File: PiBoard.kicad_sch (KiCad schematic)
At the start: 0 parts

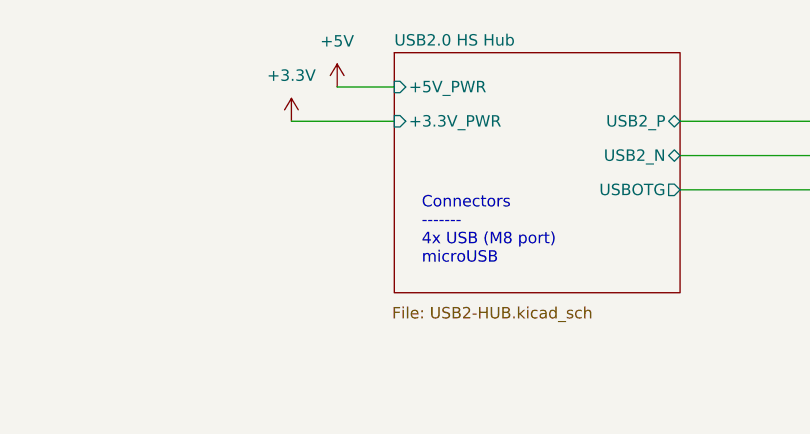
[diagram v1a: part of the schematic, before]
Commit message: fixed erc and removed old schematics
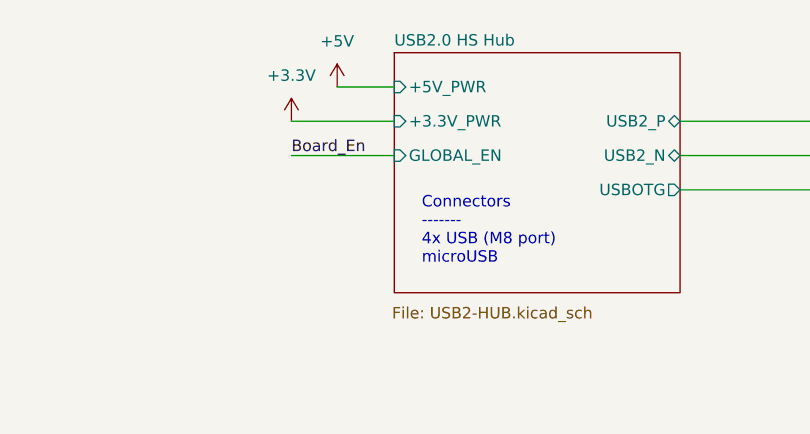
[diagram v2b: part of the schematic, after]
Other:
- sheet USB2.0 HS Hub ports: added GLOBAL_EN; removed none
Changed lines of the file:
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@@
+	(wire
+		(pts
+			(xy 133.35 45.72) (xy 121.92 45.72)
+		)
+		(stroke
+			(width 0)
+			(type default)
+		)
+	)
 	(wire
 		(pts
@@
 			(width 0)
 			(type default)
+		)
+	)
+	(label "Board_En"
+		(at 121.92 45.72 0)
+		(effects
+			(font
+				(size 1.27 1.27)
+			)
+			(justify left bottom)
 		)
 	)
@@
 			(effects
 				(font
+					(size 1.27 1.27)
+				)
+				(justify left)
+			)
+		)
+		(pin "GLOBAL_EN" input
+			(at 133.35 45.72 180)
+			(effects
+				(font

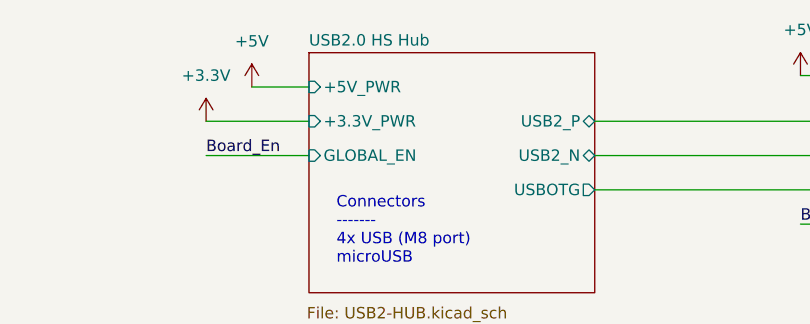
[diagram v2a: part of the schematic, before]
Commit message: changed usb to be simpler (no inbuilt hub)
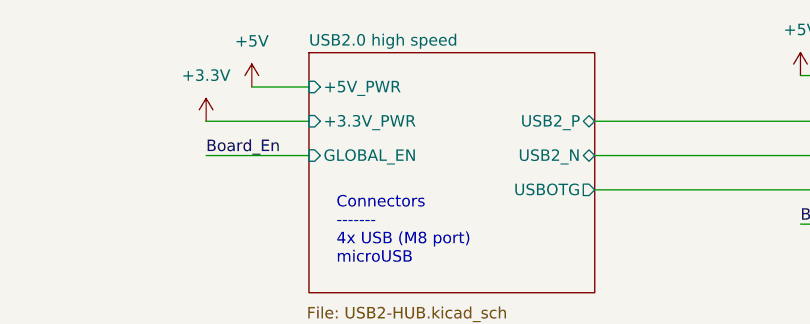
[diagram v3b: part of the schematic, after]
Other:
- sheet USB2.0 HS Hub renamed USB2.0 high speed
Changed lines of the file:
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@@
 			(color 255 255 255 0.0000)
 		)
-		(property "Sheetname" "USB2.0 HS Hub"
+		(property "Sheetname" "USB2.0 high speed"
 			(at 133.35 33.6545 0)
 			(effects

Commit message: layout draft
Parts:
- added H1, H2, H3, H4: MountingHole, MountingHole:MountingHole_3mm, symbol Mechanical:MountingHole

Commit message: my life is horrible
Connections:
- no-connect marks 1 -> 0
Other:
- removed sheet RTC and Fan
- removed sheet USB2.0 high speed
- sheet CM4 GPIO ports: added +24V_PWR, CC1, CC2; removed SCL0, SDA0, nEXTRST
- sheet HDMI and High Speed ports: added CC1, CC2; removed USB2_N, USB2_P, USBOTG_ID
- note removed: "Connectors ------- 4pin FAN"
- note removed: "Connectors ------- 4x USB (M8 port) microUSB"
- moved on the sheet: H1, H2, H3, H4

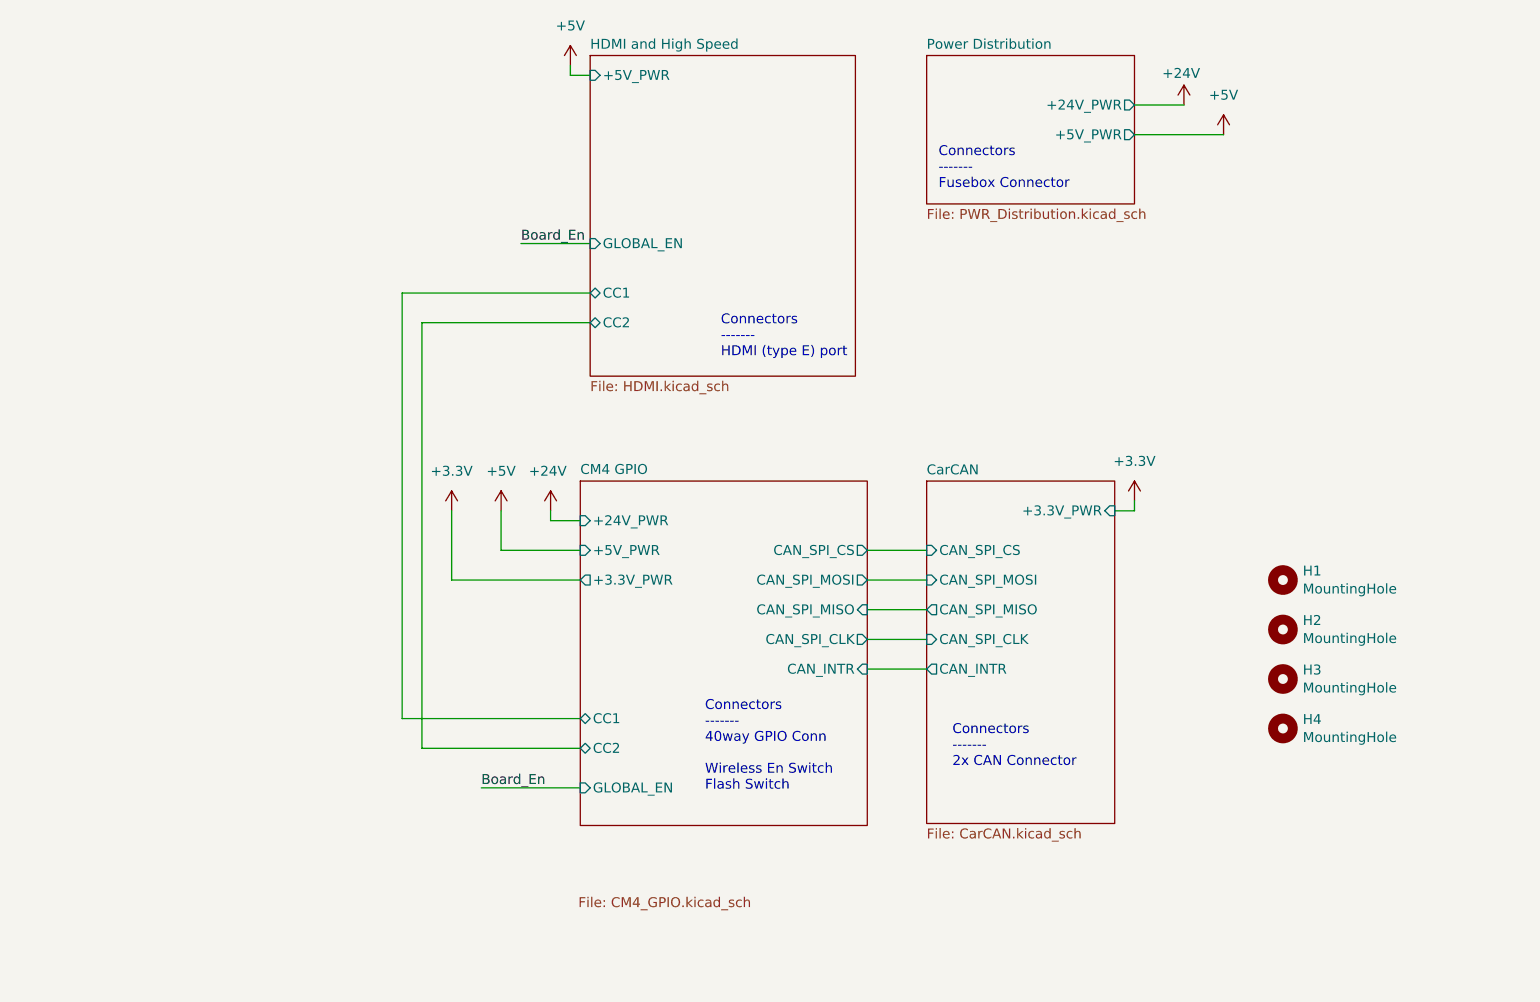
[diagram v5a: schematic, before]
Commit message: moved things to their own sheets
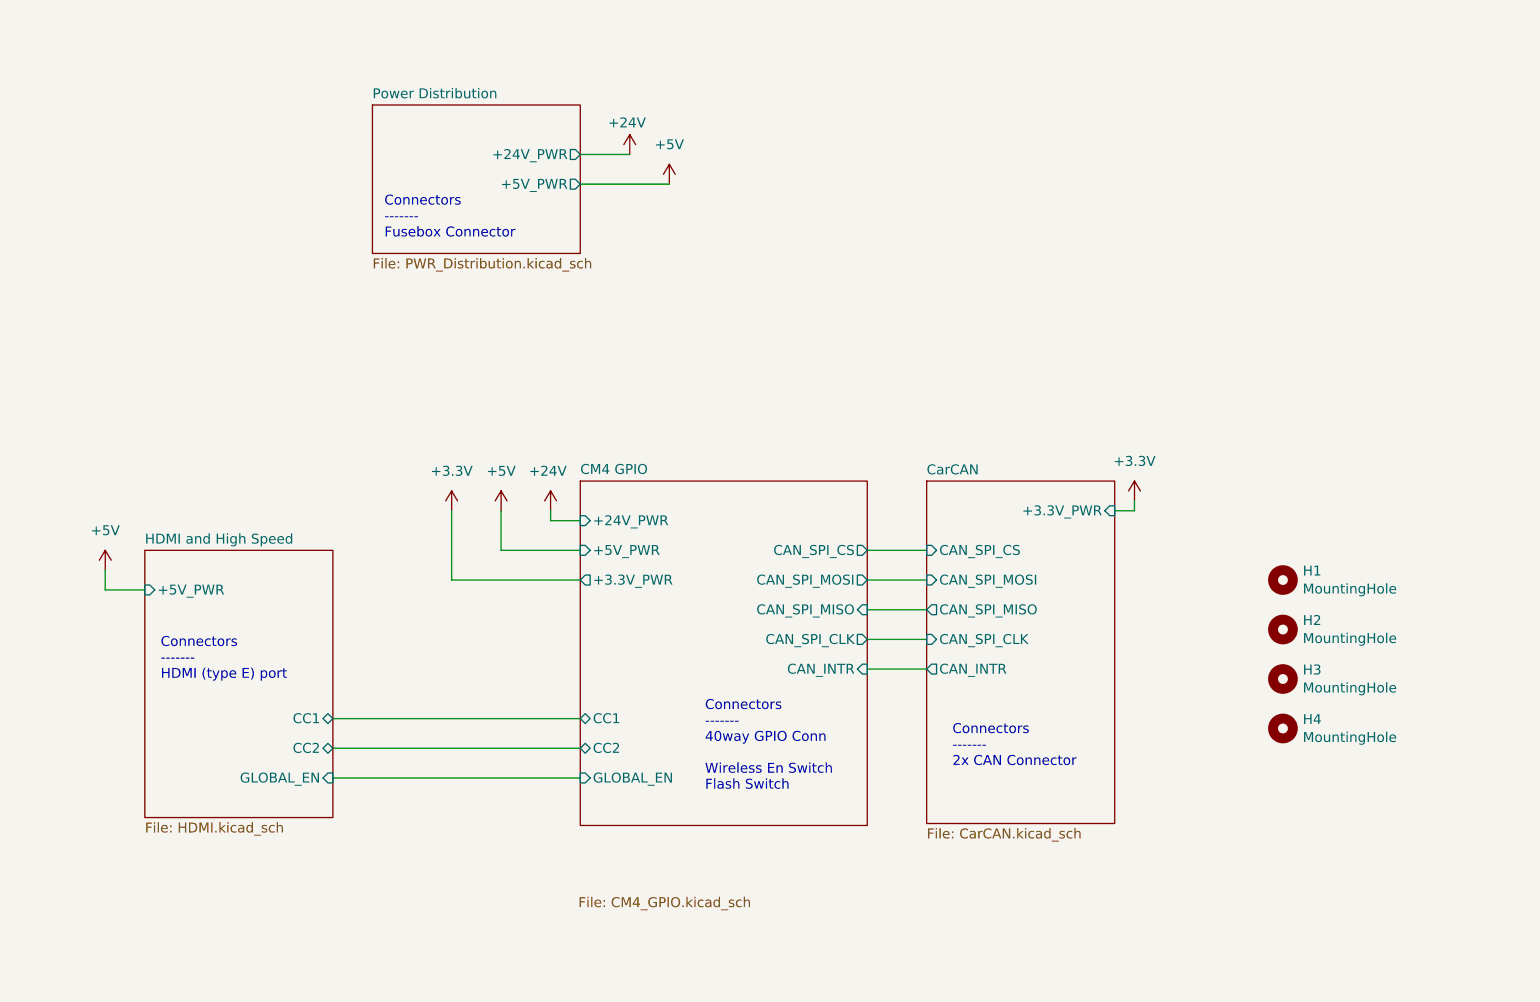
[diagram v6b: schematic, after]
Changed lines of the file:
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@@
 	(text "Connectors\n-------\nHDMI (type E) port"
 		(exclude_from_sim no)
-		(at 134.874 71.882 0)
+		(at 62.992 113.284 0)
 		(effects
 			(font
@@
 	(text "Connectors\n-------\nFusebox Connector"
 		(exclude_from_sim no)
-		(at 162.814 50.292 0)
+		(at 91.694 56.642 0)
 		(effects
 			(font
@@
 	(wire
 		(pts
-			(xy 187.96 39.37) (xy 194.31 39.37)
-		)
-		(stroke
-			(width 0)
-			(type default)
-		)
-	)
-	(wire
-		(pts
-			(xy 115.57 34.29) (xy 115.57 35.56)
-		)
-		(stroke
-			(width 0)
-			(type default)
-		)
-	)
-	(wire
-		(pts
-			(xy 96.52 121.92) (xy 96.52 67.31)
-		)
-		(stroke
-			(width 0)
-			(type default)
-		)
-	)
-	(wire
-		(pts
-			(xy 116.84 121.92) (xy 96.52 121.92)
-		)
-		(stroke
-			(width 0)
-			(type default)
-		)
-	)
-	(wire
-		(pts
-			(xy 104.14 127) (xy 116.84 127)
+			(xy 116.84 45.72) (xy 123.19 45.72)
+		)
+		(stroke
+			(width 0)
+			(type default)
+		)
+	)
+	(wire
+		(pts
+			(xy 55.88 99.06) (xy 55.88 101.6)
 		)
 		(stroke
@@
 	(wire
 		(pts
-			(xy 93.98 118.11) (xy 116.84 118.11)
-		)
-		(stroke
-			(width 0)
-			(type default)
-		)
-	)
-	(wire
-		(pts
 			(xy 113.03 91.44) (xy 113.03 92.71)
 		)
@@
 	(wire
 		(pts
-			(xy 96.52 67.31) (xy 118.11 67.31)
+			(xy 85.09 121.92) (xy 116.84 121.92)
 		)
 		(stroke
@@
 	(wire
 		(pts
-			(xy 115.57 35.56) (xy 118.11 35.56)
-		)
-		(stroke
-			(width 0)
-			(type default)
-		)
-	)
-	(wire
-		(pts
 			(xy 106.68 91.44) (xy 106.68 96.52)
 		)
@@
 	(wire
 		(pts
+			(xy 85.09 125.73) (xy 116.84 125.73)
+		)
+		(stroke
+			(width 0)
+			(type default)
+		)
+	)
+	(wire
+		(pts
 			(xy 100.33 91.44) (xy 100.33 100.33)
 		)
@@
 	(wire
 		(pts
-			(xy 187.96 43.18) (xy 199.39 43.18)
+			(xy 116.84 49.53) (xy 128.27 49.53)
+		)
+		(stroke
+			(width 0)
+			(type default)
+		)
+	)
+	(wire
+		(pts
+			(xy 60.96 101.6) (xy 55.88 101.6)
 		)
 		(stroke
@@
 	(wire
 		(pts
-			(xy 118.11 63.5) (xy 93.98 63.5)
+			(xy 85.09 118.11) (xy 116.84 118.11)
 		)
 		(stroke
@@
 	(wire
 		(pts
-			(xy 93.98 63.5) (xy 93.98 118.11)
-		)
-		(stroke
-			(width 0)
-			(type default)
-		)
-	)
-	(wire
-		(pts
 			(xy 187.96 91.44) (xy 185.42 91.44)
 		)
@@
 			(width 0)
 			(type default)
-		)
-	)
-	(wire
-		(pts
-			(xy 118.11 57.15) (xy 109.22 57.15)
-		)
-		(stroke
-			(width 0)
-			(type default)
-		)
-	)
-	(label "Board_En"
-		(at 104.14 127 0)
-		(effects
-			(font
-				(size 1.27 1.27)
-			)
-			(justify left bottom)
-		)
-	)
-	(label "Board_En"
-		(at 109.22 57.15 0)
-		(effects
-			(font
-				(size 1.27 1.27)
-			)
-			(justify left bottom)
 		)
 	)
@@
 	(symbol
 		(lib_id "power:+5V")
-		(at 199.39 43.18 0)
+		(at 128.27 49.53 0)
 		(unit 1)
 		(exclude_from_sim no)
@@
 		(fields_autoplaced yes)
 		(property "Reference" "#PWR073"
-			(at 199.39 46.99 0)
+			(at 128.27 53.34 0)
 			(effects
 				(font
@@
 		)
 		(property "Value" "+5V"
-			(at 199.39 38.1 0)
+			(at 128.27 44.45 0)
 			(effects
 				(font
@@
 		)
 		(property "Footprint" ""
-			(at 199.39 43.18 0)
+			(at 128.27 49.53 0)
 			(effects
 				(font
@@
 		)
 		(property "Datasheet" ""
-			(at 199.39 43.18 0)
+			(at 128.27 49.53 0)
 			(effects
 				(font
@@
 		)
 		(property "Description" "Power symbol creates a global label with name \"+5V\""
-			(at 199.39 43.18 0)
+			(at 128.27 49.53 0)
 			(effects
 				(font
@@
 	(symbol
 		(lib_id "power:+5V")
-		(at 115.57 34.29 0)
+		(at 55.88 99.06 0)
 		(unit 1)
 		(exclude_from_sim no)
@@
 		(fields_autoplaced yes)
 		(property "Reference" "#PWR076"
-			(at 115.57 38.1 0)
+			(at 55.88 102.87 0)
 			(effects
 				(font
@@
 		)
 		(property "Value" "+5V"
-			(at 115.57 29.21 0)
+			(at 55.88 93.98 0)
 			(effects
 				(font
@@
 		)
 		(property "Footprint" ""
-			(at 115.57 34.29 0)
+			(at 55.88 99.06 0)
 			(effects
 				(font
@@
 		)
 		(property "Datasheet" ""
-			(at 115.57 34.29 0)
+			(at 55.88 99.06 0)
 			(effects
 				(font
@@
 		)
 		(property "Description" "Power symbol creates a global label with name \"+5V\""
-			(at 115.57 34.29 0)
+			(at 55.88 99.06 0)
 			(effects
 				(font
@@
 	(symbol
 		(lib_id "power:+12V")
-		(at 194.31 39.37 0)
+		(at 123.19 45.72 0)
 		(unit 1)
 		(exclude_from_sim no)
@@
 		(dnp no)
 		(property "Reference" "#PWR066"
-			(at 194.31 43.18 0)
+			(at 123.19 49.53 0)
 			(effects
 				(font
@@
 		)
 		(property "Value" "+24V"
-			(at 191.516 35.306 0)
+			(at 120.396 41.656 0)
 			(effects
 				(font
@@
 		)
 		(property "Footprint" ""
-			(at 194.31 39.37 0)
+			(at 123.19 45.72 0)
 			(effects
 				(font
@@
 		)
 		(property "Datasheet" ""
-			(at 194.31 39.37 0)
+			(at 123.19 45.72 0)
 			(effects
 				(font
@@
 		)
 		(property "Description" "Power symbol creates a global label with name \"+12V\""
-			(at 194.31 39.37 0)
+			(at 123.19 45.72 0)
 			(effects
 				(font
@@
 	)
 	(sheet
-		(at 161.29 33.02)
+		(at 90.17 39.37)
 		(size 26.67 19.05)
 		(exclude_from_sim no)
@@
 		)
 		(property "Sheetname" "Power Distribution"
-			(at 161.29 32.3084 0)
+			(at 90.17 38.6584 0)
 			(effects
 				(font
@@
 		)
 		(property "Sheetfile" "PWR_Distribution.kicad_sch"
-			(at 161.29 52.6546 0)
+			(at 90.17 59.0046 0)
 			(effects
 				(font
@@
 		)
 		(pin "+5V_PWR" output
-			(at 187.96 43.18 0)
+			(at 116.84 49.53 0)
 			(effects
 				(font
@@
 		)
 		(pin "+24V_PWR" output
-			(at 187.96 39.37 0)
+			(at 116.84 45.72 0)
 			(effects
 				(font
@@
 	)
 	(sheet
-		(at 118.11 33.02)
-		(size 34.036 41.148)
+		(at 60.96 96.52)
+		(size 24.13 34.29)
 		(exclude_from_sim no)
 		(in_bom yes)
@@
 		)
 		(property "Sheetname" "HDMI and High Speed"
-			(at 118.11 32.3084 0)
+			(at 60.96 95.8084 0)
 			(effects
 				(font
@@
 		)
 		(property "Sheetfile" "HDMI.kicad_sch"
-			(at 118.11 74.7526 0)
+			(at 60.96 131.3946 0)
 			(effects
 				(font
@@
 		)
 		(pin "+5V_PWR" input
-			(at 118.11 35.56 180)
+			(at 60.96 101.6 180)
 			(effects
 				(font
@@
 		)
 		(pin "GLOBAL_EN" input
-			(at 118.11 57.15 180)
-			(effects
-				(font
-					(size 1.27 1.27)
-				)
-				(justify left)
+			(at 85.09 125.73 0)
+			(effects
+				(font
+					(size 1.27 1.27)
+				)
+				(justify right)
 			)
 		)
 		(pin "CC1" bidirectional
-			(at 118.11 63.5 180)
-			(effects
-				(font
-					(size 1.27 1.27)
-				)
-				(justify left)
+			(at 85.09 118.11 0)
+			(effects
+				(font
+					(size 1.27 1.27)
+				)
+				(justify right)
 			)
 		)
 		(pin "CC2" bidirectional
-			(at 118.11 67.31 180)
-			(effects
-				(font
-					(size 1.27 1.27)
-				)
-				(justify left)
+			(at 85.09 121.92 0)
+			(effects
+				(font
+					(size 1.27 1.27)
+				)
+				(justify right)
 			)
 		)
@@
 		)
 		(pin "GLOBAL_EN" input
-			(at 116.84 127 180)
-			(effects
-				(font
+			(at 116.84 125.73 180)
+			(effects
+				(font

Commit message: rrrrrrrr
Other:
- sheet CM4 GPIO renamed CM5 GPIO
- sheet HDMI and High Speed renamed High Speed
- sheet CM5 GPIO: file CM4_GPIO.kicad_sch -> CM5_GPIO.kicad_sch
- sheet High Speed: file HDMI.kicad_sch -> CM5_HighSpeed.kicad_sch
- note added: "Connectors ------- HDMI (type E) port USB C 3.0 (HUB) USB C 2.0 (DBG) USB C 2.0 (PWR)"
- note removed: "Connectors ------- HDMI (type E) port"
- moved on the sheet: H1, H2, H3, H4

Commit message: Schem done? [plz full review], redoing layout
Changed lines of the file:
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@@
 	(text "Connectors\n-------\nFusebox Connector"
 		(exclude_from_sim no)
-		(at 86.614 71.882 0)
+		(at 87.884 71.882 0)
 		(effects
 			(font
@@
 	(wire
 		(pts
-			(xy 111.76 60.96) (xy 118.11 60.96)
+			(xy 113.03 60.96) (xy 119.38 60.96)
 		)
 		(stroke
@@
 	(wire
 		(pts
-			(xy 111.76 64.77) (xy 123.19 64.77)
+			(xy 113.03 64.77) (xy 124.46 64.77)
 		)
 		(stroke
@@
 	(symbol
 		(lib_id "power:+5V")
-		(at 123.19 64.77 0)
+		(at 124.46 64.77 0)
 		(unit 1)
 		(exclude_from_sim no)
@@
 		(fields_autoplaced yes)
 		(property "Reference" "#PWR073"
-			(at 123.19 68.58 0)
+			(at 124.46 68.58 0)
 			(effects
 				(font
@@
 		)
 		(property "Value" "+5V"
-			(at 123.19 59.69 0)
+			(at 124.46 59.69 0)
 			(effects
 				(font
@@
 		)
 		(property "Footprint" ""
-			(at 123.19 64.77 0)
+			(at 124.46 64.77 0)
 			(effects
 				(font
@@
 		)
 		(property "Datasheet" ""
-			(at 123.19 64.77 0)
+			(at 124.46 64.77 0)
 			(effects
 				(font
@@
 		)
 		(property "Description" "Power symbol creates a global label with name \"+5V\""
-			(at 123.19 64.77 0)
+			(at 124.46 64.77 0)
 			(effects
 				(font
@@
 	(symbol
 		(lib_id "power:+12V")
-		(at 118.11 60.96 0)
+		(at 119.38 60.96 0)
 		(unit 1)
 		(exclude_from_sim no)
@@
 		(dnp no)
 		(property "Reference" "#PWR066"
-			(at 118.11 64.77 0)
+			(at 119.38 64.77 0)
 			(effects
 				(font
@@
 		)
 		(property "Value" "+24V"
-			(at 115.316 56.896 0)
+			(at 116.586 56.896 0)
 			(effects
 				(font
@@
 		)
 		(property "Footprint" ""
-			(at 118.11 60.96 0)
+			(at 119.38 60.96 0)
 			(effects
 				(font
@@
 		)
 		(property "Datasheet" ""
-			(at 118.11 60.96 0)
+			(at 119.38 60.96 0)
 			(effects
 				(font
@@
 		)
 		(property "Description" "Power symbol creates a global label with name \"+12V\""
-			(at 118.11 60.96 0)
+			(at 119.38 60.96 0)
 			(effects
 				(font
@@
 	)
 	(sheet
-		(at 85.09 54.61)
+		(at 86.36 54.61)
 		(size 26.67 19.05)
 		(exclude_from_sim no)
@@
 		)
 		(property "Sheetname" "Power Distribution"
-			(at 85.09 53.8984 0)
+			(at 86.36 53.8984 0)
 			(effects
 				(font
@@
 		)
 		(property "Sheetfile" "PWR_Distribution.kicad_sch"
-			(at 85.09 74.2446 0)
+			(at 86.36 74.2446 0)
 			(effects
 				(font
@@
 		)
 		(pin "+5V_PWR" output
-			(at 111.76 64.77 0)
+			(at 113.03 64.77 0)
 			(effects
 				(font
@@
 		)
 		(pin "+24V_PWR" output
-			(at 111.76 60.96 0)
-			(effects
-				(font
+			(at 113.03 60.96 0)
+			(effects
+				(font
